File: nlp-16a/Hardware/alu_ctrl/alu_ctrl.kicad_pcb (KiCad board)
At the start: 2 copper layers, 209.5 x 154.9 mm, 112 parts, among them J1 Screw_Terminal_01x02, J10 Conn_02x08_Odd_Even, J2 Conn_02x20_Odd_Even, J3 Conn_02x10_Counter_Clockwise, J4 Conn_02x10_Counter_Clockwise, J5 Conn_02x10_Counter_Clockwise, J6 Conn_02x10_Counter_Clockwise, J7 Conn_02x10_Counter_Clockwise, J8 Conn_02x08_Odd_Even, J9 Conn_02x08_Odd_Even, U1 CD74HC00, U10 CD74HC00, U11 CD74HC00, U12 CD74HC00, U13 CD74HC00, U14 CD74HC00, U15 CD74HC00, U16 CD74HC00, U17 CD74HC00, U18 CD74HC00, U19 CD74HC00, U2 CD74HC00, U20 CD74HC00, U21 CD74HC00, U22 CD74HC00, U23 CD74HC00, U24 CD74HC00, U25 CD74HC00, U26 CD74HC00, U27 CD74HC00, U28 CD74HC00, U3 CD74HC00, U4 CD74HC00, U5 CD74HC00, U6 CD74HC00, U7 CD74HC00, U8 CD74HC00, U9 CD74HC00

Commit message: コミット漏れていた
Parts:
- moved J10 110.3 mm to (27.9, 80.0), turned to 180 degrees
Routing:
- net VCC: track 1154.0 -> 1152.7 mm

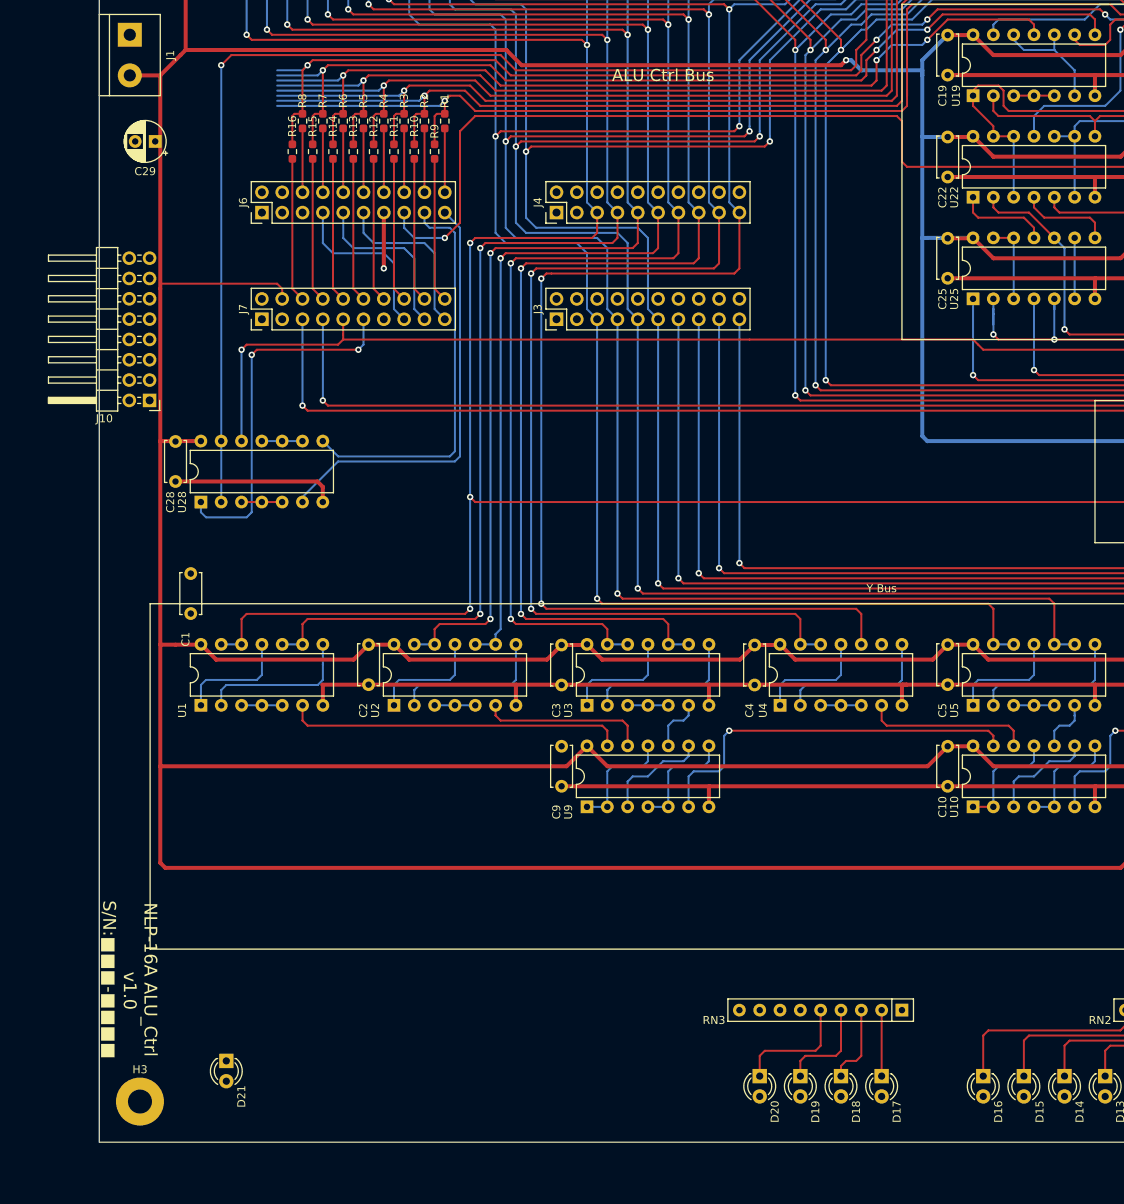
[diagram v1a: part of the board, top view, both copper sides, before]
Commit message: デバッグポート(ALU制御バス)の配置プランが立った
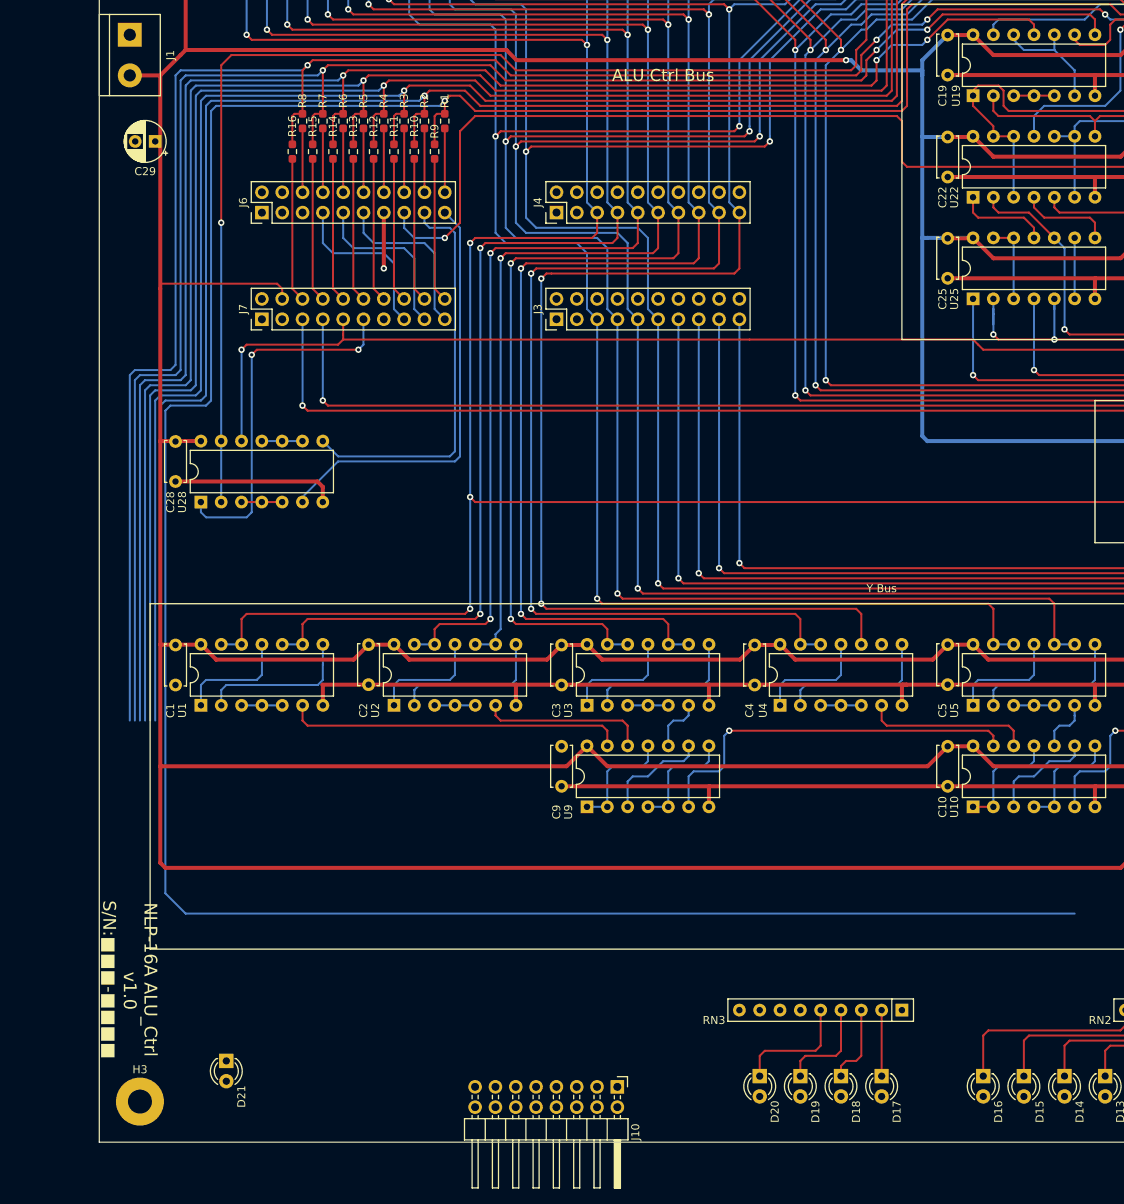
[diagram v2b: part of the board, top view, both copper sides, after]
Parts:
- moved J10 103.8 mm to (86.3, 165.8), turned to -90 degrees
- moved C1 9.13 mm to (31.1, 115.6)
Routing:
- net ADD/SUB: track 343.7 -> 569.7 mm
- net ALU_Ctrl7: track 141.1 -> 239.7 mm
- net ALU_Ctrl6: track 120.6 -> 217.9 mm
- net ALU_Ctrl5: track 112.1 -> 208.1 mm
- net ALU_Ctrl4: track 155.3 -> 250.1 mm
- net ALU_Ctrl3: track 146.1 -> 239.6 mm
- net ALU_Ctrl2: track 165.0 -> 257.2 mm
- net ALU_Ctrl1: track 174.9 -> 265.9 mm
- net VCC: track 1152.7 -> 1152.2 mm

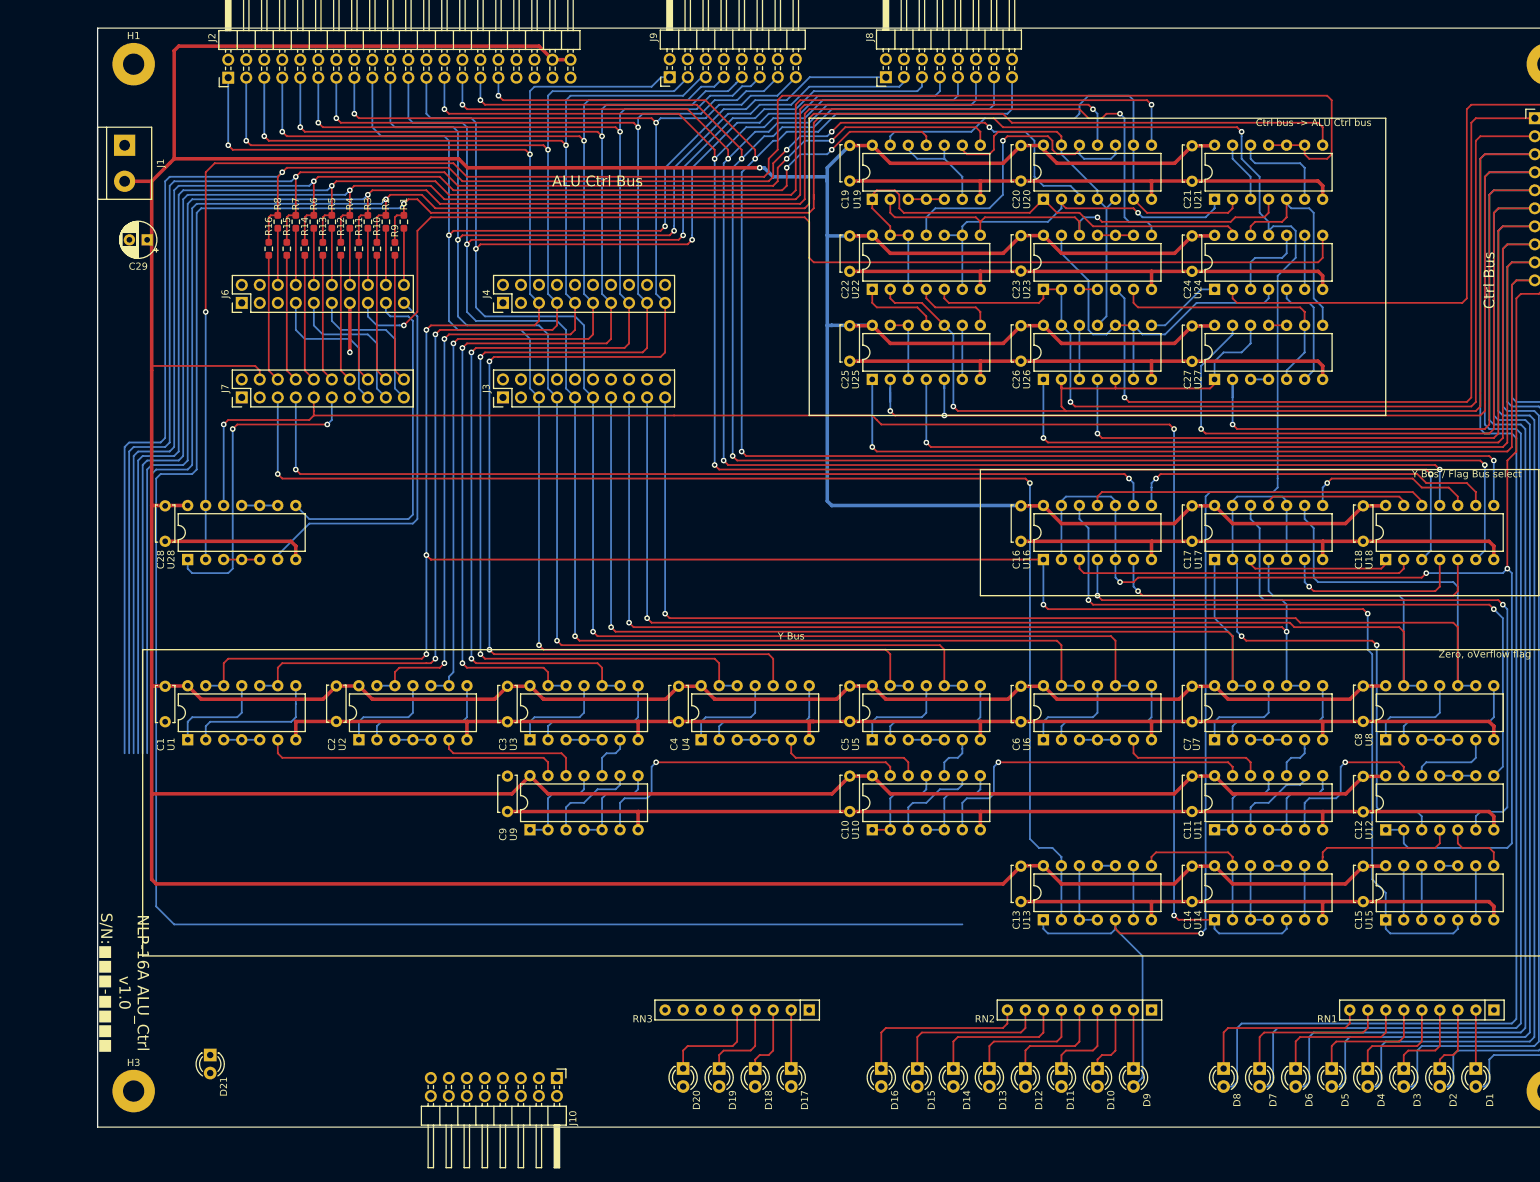
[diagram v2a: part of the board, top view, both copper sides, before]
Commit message: 電源バスの引き直しとデバッグポートの配線完了
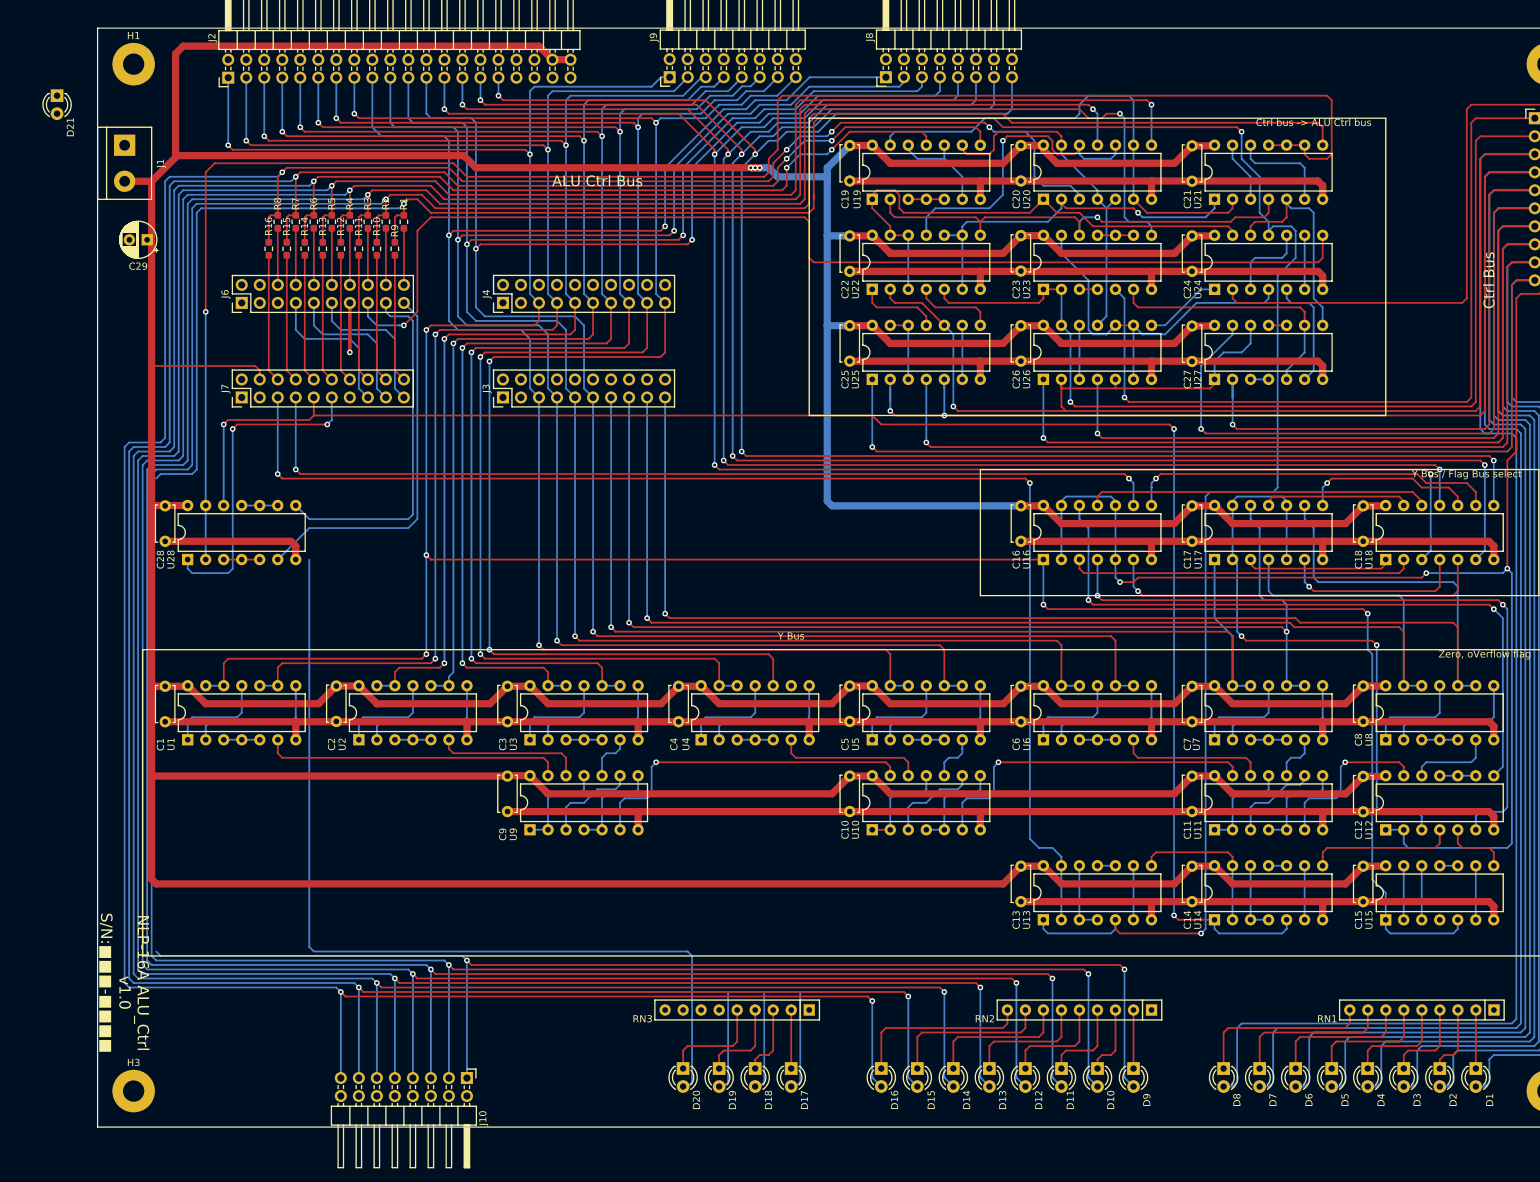
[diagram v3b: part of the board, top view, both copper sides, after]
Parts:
- moved D21 137.0 mm to (15.9, 27.3)
- moved J10 12.7 mm to (73.7, 165.8)
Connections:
- J10 pad 1: unconnected-(J10-Pad1) -> ADD/SUB
- J10 pad 11: Z -> ALU_Ctrl5
- J10 pad 13: V -> ALU_Ctrl6
- J10 pad 15: Y_BUS15 -> ALU_Ctrl7
- J10 pad 3: unconnected-(J10-Pad3) -> ALU_Ctrl1
- J10 pad 5: unconnected-(J10-Pad5) -> ALU_Ctrl2
- J10 pad 7: Cin -> ALU_Ctrl3
- J10 pad 9: C -> ALU_Ctrl4
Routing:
- net ALU_Ctrl1: track 265.9 -> 459.9 mm, vias 1 -> 3
- net ALU_Ctrl2: track 257.2 -> 446.2 mm, vias 2 -> 4
- net ALU_Ctrl3: track 239.6 -> 423.4 mm, vias 2 -> 4
- net ALU_Ctrl4: track 250.1 -> 428.9 mm, vias 2 -> 4
- net ALU_Ctrl5: track 208.1 -> 381.8 mm, vias 3 -> 5
- net ALU_Ctrl6: track 217.9 -> 386.6 mm, vias 3 -> 5
- net ALU_Ctrl7: track 239.7 -> 403.3 mm, vias 4 -> 6
- net C: track 132.2 -> 260.6 mm
- net ADD/SUB: track 569.7 -> 541.6 mm, vias 3 -> 5
- net GND: track 736.4 -> 753.9 mm
- net Y_BUS15: track 400.3 -> 415.2 mm
- net V: track 98.5 -> 112.7 mm
- net Z: track 96.2 -> 110.4 mm
- net VCC: track 1152.2 -> 1152.5 mm, vias 1 -> 3

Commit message: だいたい完成．残りは詳細チェックとビア打ち
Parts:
- moved D21 138.4 mm to (34.3, 164.5)
- moved R17 120.6 mm to (38.1, 164.5), turned to -90 degrees
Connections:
- D18 pad 2: V -> Z
- D19 pad 2: Z -> V
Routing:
- net V: track 112.7 -> 222.2 mm, vias 2 -> 3
- net Z: track 110.4 -> 212.0 mm, vias 2 -> 3
- net Y_BUS15: track 415.2 -> 503.2 mm, vias 7 -> 8
- net ADD/SUB: track 541.6 -> 606.6 mm
- net VCC: track 1152.5 -> 1176.6 mm, vias 3 -> 2
- net Lout/A_sign: track 244.7 -> 264.3 mm
- net C: track 260.6 -> 279.9 mm
- net Net-(D21-Pad2): track 0.00 -> 4.96 mm
- net Y_BUS8: track 213.7 -> 216.2 mm
- net Net-(U15-Pad12): track 7.62 -> 10.2 mm
- net Ctrl5: track 252.1 -> 250.2 mm
- net Ctrl6: track 313.0 -> 311.8 mm
- net Net-(U17-Pad8): track 25.1 -> 24.4 mm
- net ROLL: track 243.8 -> 243.2 mm
- net GND: vias 1 -> 426
- added copper zone on B.Cu, net GND
- added copper zone on F.Cu, net GND

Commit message: ALU制御基板OK
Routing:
- net GND: vias 426 -> 565
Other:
- board text added: "+ -"
- board text added: "0 ------------ 7"
- board text added: "0 ------------------------------------- F"
- board text added: "7 0"
- board text added: "8 ------------ F"
- board text added: "ALU Ctrl BUS"
- board text added: "ALU Y BUS"
- board text added: "C V Z S"
- board text added: "Ctrl BUS"
- board text added: "DEBUG PORT(ALU Ctrl)"
- board text added: "DEBUG PORT(Y/Flag)"
- board text added: "PWR"
- board text added: "Y BUS"
- board text removed: "ALU Ctrl Bus"
- board text removed: "Ctrl Bus"
- board text removed: "Y Bus"
